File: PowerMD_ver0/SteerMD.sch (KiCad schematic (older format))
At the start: 216 parts, among them P1 SWD, P10 OUT_1, P11 ENC_0, P13 ENC_1, P14 I/O_1, P15 OUT_0, P2 MOTOR_COOLING, P3 CAN, P4 CAN, P5 SERIAL, P6 I/O_0, P7 FAN, P8 BATT_IN, P9 BATT_IN, Q1 MOSFET_N, Q2 MOSFET_N, Q3 MOSFET_N, Q4 MOSFET_N, Q5 MOSFET_N, Q6 MOSFET_N, Q7 MOSFET_N, Q8 MOSFET_N, SW1 RST, SW3 SW0, SW4 SW1, U1 MAX3051, U10 ACS758, U11 POWER_ON, U12 SI8274, U13 ACS758, U14 SI8274, U15 AZ1086H, U16 LOGO, U17 AQM0802, U19 ADRESS, U2 BD9G101, U3 STM32F405RG, U4 SI8274, U5 SI8900, U6 ADC_~RST, U7 BD9G101G, U8 SI8274, U9 BD33FA1, Y1 8MHz

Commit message: ねむねむ。( ˘ω˘)ｽﾔｧ
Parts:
- R19, R20, R28, R29, R55, R56, R58, R59: value 1 -> 10
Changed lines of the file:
@@
 P 13425 9300
 F 0 "R59" V 13218 9300 50  0000 C CNN
-F 1 "1" V 13309 9300 50  0000 C CNN
+F 1 "10" V 13309 9300 50  0000 C CNN
 F 2 "Mizz_lib:1608_WP" V 13355 9300 50  0001 C CNN
 F 3 "~" H 13425 9300 50  0001 C CNN
@@
 P 13425 8550
 F 0 "R58" V 13218 8550 50  0000 C CNN
-F 1 "1" V 13309 8550 50  0000 C CNN
+F 1 "10" V 13309 8550 50  0000 C CNN
 F 2 "Mizz_lib:1608_WP" V 13355 8550 50  0001 C CNN
 F 3 "~" H 13425 8550 50  0001 C CNN
@@
 P 11475 9300
 F 0 "R56" V 11268 9300 50  0000 C CNN
-F 1 "1" V 11359 9300 50  0000 C CNN
+F 1 "10" V 11359 9300 50  0000 C CNN
 F 2 "Mizz_lib:1608_WP" V 11405 9300 50  0001 C CNN
 F 3 "~" H 11475 9300 50  0001 C CNN
@@
 P 11475 8550
 F 0 "R55" V 11268 8550 50  0000 C CNN
-F 1 "1" V 11359 8550 50  0000 C CNN
+F 1 "10" V 11359 8550 50  0000 C CNN
 F 2 "Mizz_lib:1608_WP" V 11405 8550 50  0001 C CNN
 F 3 "~" H 11475 8550 50  0001 C CNN
@@
 P 13425 6825
 F 0 "R29" V 13218 6825 50  0000 C CNN
-F 1 "1" V 13309 6825 50  0000 C CNN
+F 1 "10" V 13309 6825 50  0000 C CNN
 F 2 "Mizz_lib:1608_WP" V 13355 6825 50  0001 C CNN
 F 3 "~" H 13425 6825 50  0001 C CNN
@@
 P 13425 6075
 F 0 "R28" V 13218 6075 50  0000 C CNN
-F 1 "1" V 13309 6075 50  0000 C CNN
+F 1 "10" V 13309 6075 50  0000 C CNN
 F 2 "Mizz_lib:1608_WP" V 13355 6075 50  0001 C CNN
 F 3 "~" H 13425 6075 50  0001 C CNN
@@
 P 11475 6825
 F 0 "R20" V 11268 6825 50  0000 C CNN
-F 1 "1" V 11359 6825 50  0000 C CNN
+F 1 "10" V 11359 6825 50  0000 C CNN
 F 2 "Mizz_lib:1608_WP" V 11405 6825 50  0001 C CNN
 F 3 "~" H 11475 6825 50  0001 C CNN
@@
 P 11475 6075
 F 0 "R19" V 11268 6075 50  0000 C CNN
-F 1 "1" V 11359 6075 50  0000 C CNN
+F 1 "10" V 11359 6075 50  0000 C CNN
 F 2 "Mizz_lib:1608_WP" V 11405 6075 50  0001 C CNN
 F 3 "~" H 11475 6075 50  0001 C CNN

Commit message: 電流制御MD(仮)配線(仮)完成(仮)
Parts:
- R37: value 50k -> 3.9k
- R38: value 10k -> 680
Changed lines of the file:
@@
 P 3275 1450
 F 0 "R37" H 3345 1496 50  0000 L CNN
-F 1 "50k" H 3345 1405 50  0000 L CNN
+F 1 "3.9k" H 3345 1405 50  0000 L CNN
 F 2 "Resistor_SMD:R_0603_1608Metric" V 3205 1450 50  0001 C CNN
 F 3 "~" H 3275 1450 50  0001 C CNN
@@
 P 3275 1800
 F 0 "R38" H 3345 1846 50  0000 L CNN
-F 1 "10k" H 3345 1755 50  0000 L CNN
+F 1 "680" H 3345 1755 50  0000 L CNN
 F 2 "Resistor_SMD:R_0603_1608Metric" V 3205 1800 50  0001 C CNN
 F 3 "~" H 3275 1800 50  0001 C CNN

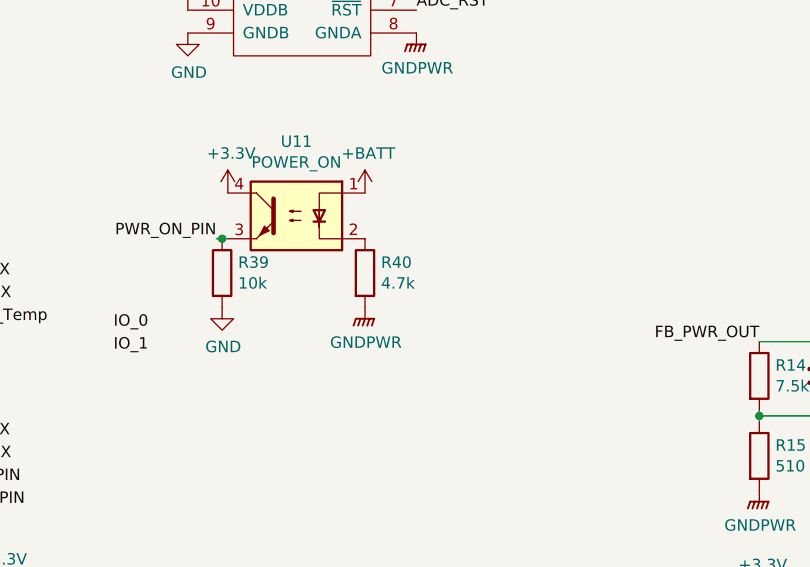
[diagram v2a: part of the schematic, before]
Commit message: 抵抗値を実装されているものに変更した
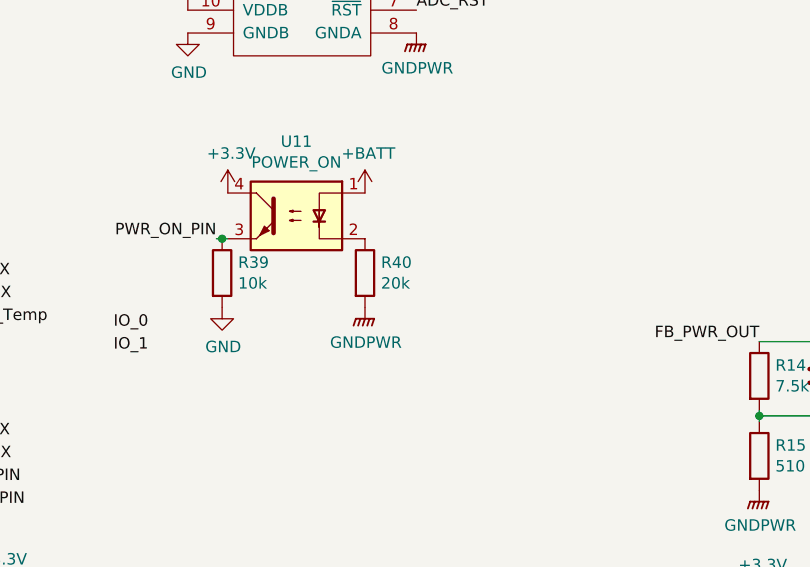
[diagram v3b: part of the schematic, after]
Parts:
- R40: value 4.7k -> 20k
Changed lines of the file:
@@
 EESchema Schematic File Version 4
-LIBS:SteerMD-cache
 EELAYER 30 0
 EELAYER END
@@
 P 8850 3625
 F 0 "R40" H 8920 3671 50  0000 L CNN
-F 1 "4.7k" H 8920 3580 50  0000 L CNN
+F 1 "20k" H 8920 3580 50  0000 L CNN
 F 2 "Resistor_SMD:R_0603_1608Metric" V 8780 3625 50  0001 C CNN
 F 3 "~" H 8850 3625 50  0001 C CNN

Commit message: MD,12V出力回路変更
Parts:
- JP3: footprint Mizz_lib:SW_Micro_SPST -> Connector_PinHeader_2.54mm:PinHeader_1x03_P2.54mm_Vertical
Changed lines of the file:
@@
 F 0 "JP3" H 5850 11099 50  0000 C CNN
 F 1 "I/O_Vdd" H 5850 11008 50  0000 C CNN
-F 2 "Mizz_lib:SW_Micro_SPST" H 5850 10875 50  0001 C CNN
+F 2 "Connector_PinHeader_2.54mm:PinHeader_1x03_P2.54mm_Vertical" H 5850 10875 50  0001 C CNN
 F 3 "~" H 5850 10875 50  0001 C CNN
 	1    5850 10875
